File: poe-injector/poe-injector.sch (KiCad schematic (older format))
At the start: 41 parts, among them IC1 ATTINY44-SS, J1 AVRISP6, J2 RJCSE538001, J3 RJCSE538001, Q1 SQ2361EES, Q2 2N7002K, Q3 SQ2361EES, Q4 2N7002K, U2 LTC6101, U4 LTC6101

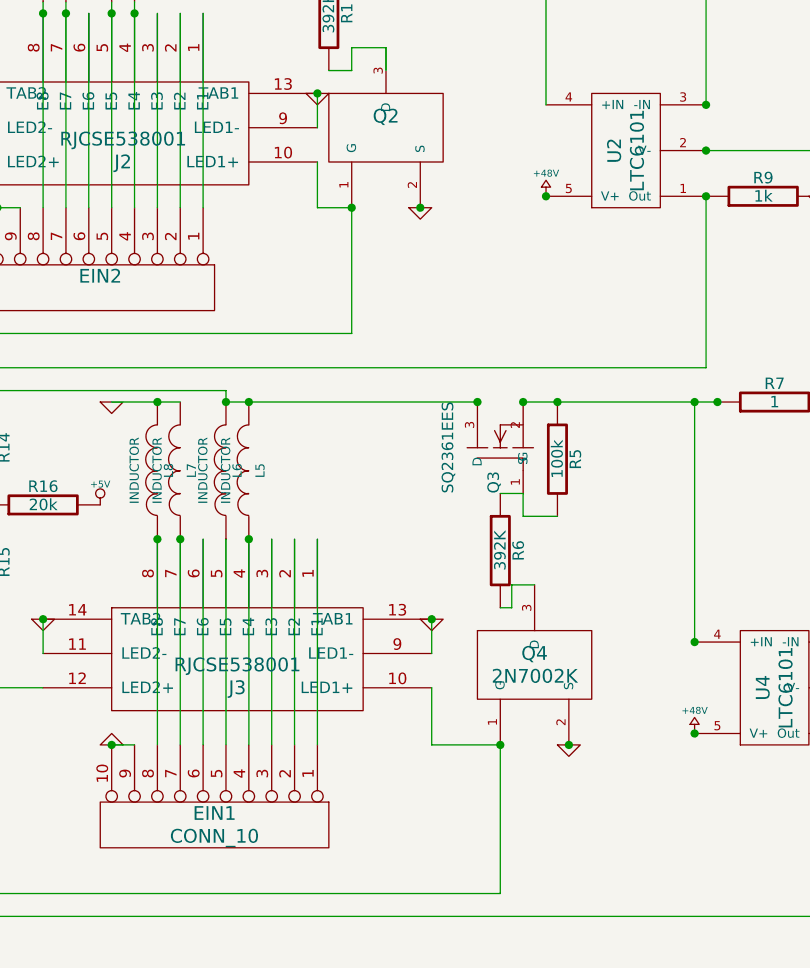
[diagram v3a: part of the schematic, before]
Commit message: Add current-limiting resistors for LEDs, not sure on placement :(
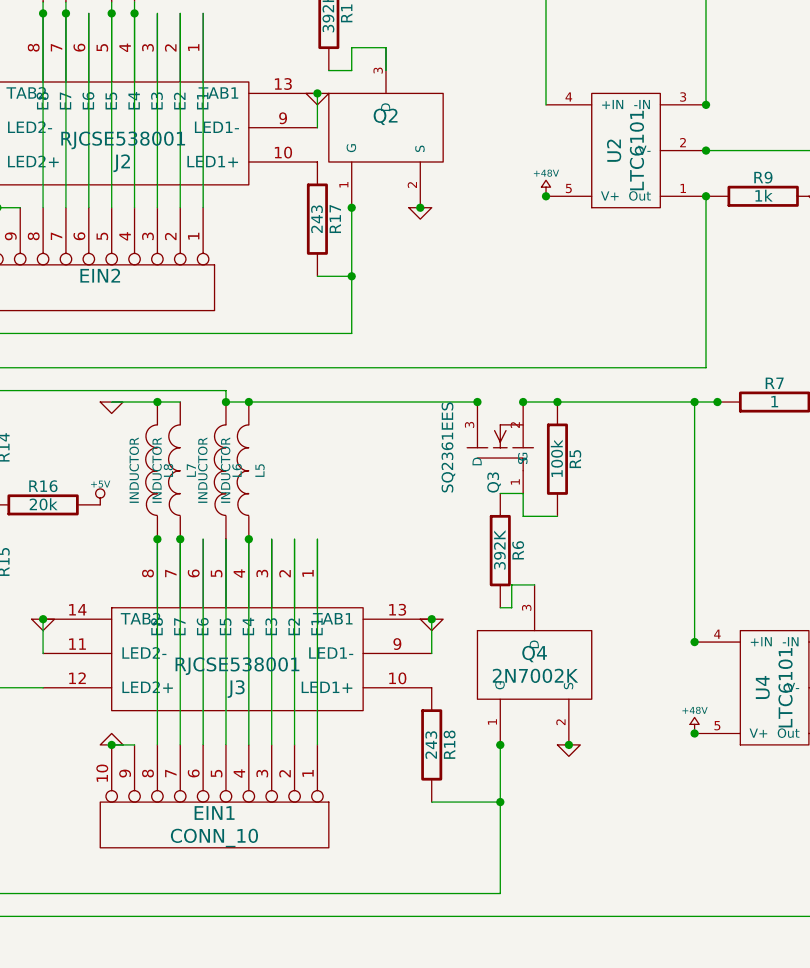
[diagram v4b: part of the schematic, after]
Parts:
- added R17, R18: 243, symbol R
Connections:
- net at IC1.3 ((PCINT9/XTAL2)PB1), Q2.1 (G): now also R17.2; no longer J2.10 (LED1+)
- net at IC1.5 ((PCINT10/CKOUT/OC0A/INT0)PB2), Q4.1 (G): now also R18.2; no longer J3.10 (LED1+)
- new net: J2.10 (LED1+), R17.1
- new net: J3.10 (LED1+), R18.1
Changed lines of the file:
@@
-EESchema Schematic File Version 2  date 3/14/2013 6:43:47 PM
+EESchema Schematic File Version 2  date 3/14/2013 8:06:13 PM
 LIBS:power
 LIBS:device
@@
 Sheet 1 1
 Title ""
-Date "14 mar 2013"
+Date "15 mar 2013"
 Rev ""
 Comp ""
@@
 Comment4 ""
 $EndDescr
+Connection ~ 6250 3050
+Wire Wire Line
+	6100 3050 6250 3050
 Wire Wire Line
 	6250 2050 6400 2050
@@
 Connection ~ 6100 2250
 Wire Wire Line
-	6100 2550 6100 2750
-Wire Wire Line
-	6100 2750 6250 2750
-Wire Wire Line
 	6600 4550 6600 4700
-Wire Wire Line
-	6600 4850 6600 5100
-Wire Wire Line
-	6600 5100 6900 5100
 Wire Wire Line
 	7800 2700 7800 3450
@@
 	6450 1650 6150 1650
 Connection ~ 6350 1650
+Wire Wire Line
+	6600 5350 6900 5350
+Connection ~ 6900 5350
+$Comp
+L R R17
+U 1 1 51426593
+P 6100 2800
+F 0 "R17" V 6180 2800 50  0000 C CNN
+F 1 "243" V 6100 2800 50  0000 C CNN
+	1    6100 2800
+	1    0    0    -1
+$EndComp
+$Comp
+L R R18
+U 1 1 5142658A
+P 6600 5100
+F 0 "R18" V 6680 5100 50  0000 C CNN
+F 1 "243" V 6600 5100 50  0000 C CNN
+	1    6600 5100
+	1    0    0    -1
+$EndComp
 $Comp
 L GND #PWR01
